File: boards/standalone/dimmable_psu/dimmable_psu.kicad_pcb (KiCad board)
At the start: 2 copper layers, 78 parts, among them J1 DIM_IN, J2 PWM_IN, J3 POWER, J4 POWER_OUT, Q1 2N7002, Q2 IRF540N, Q3 IRF540N, U1 LM324, U2 LMC7660, U3 TPS92640

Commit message: proper footprint for opamp
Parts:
- U1: footprint Package_SO:SO-14_3.9x8.65mm_P1.27mm -> Package_SO:SOIC-14_3.9x8.7mm_P1.27mm

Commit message: mounting holes!
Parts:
- added H1: MountingHole_Pad, MountingHole:MountingHole_3.2mm_M3_Pad, F.Cu at (4.00, 4.00)
- added H2: MountingHole_Pad, MountingHole:MountingHole_3.2mm_M3_Pad, F.Cu at (96.0, 4.00)
- added H3: MountingHole_Pad, MountingHole:MountingHole_3.2mm_M3_Pad, F.Cu at (96.0, 46.0)
- added H4: MountingHole_Pad, MountingHole:MountingHole_3.2mm_M3_Pad, F.Cu at (4.00, 46.0)
- moved C2 147.9 mm to (27.7, 36.0)
- moved J1 147.9 mm to (10.7, 22.0)
- moved J2 147.9 mm to (10.7, 14.5)
- moved J3 147.9 mm to (8.24, 33.0)
- moved L1 51.9 mm to (82.0, 25.0), turned to 90 degrees
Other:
- board outline added: 100 x 50 mm

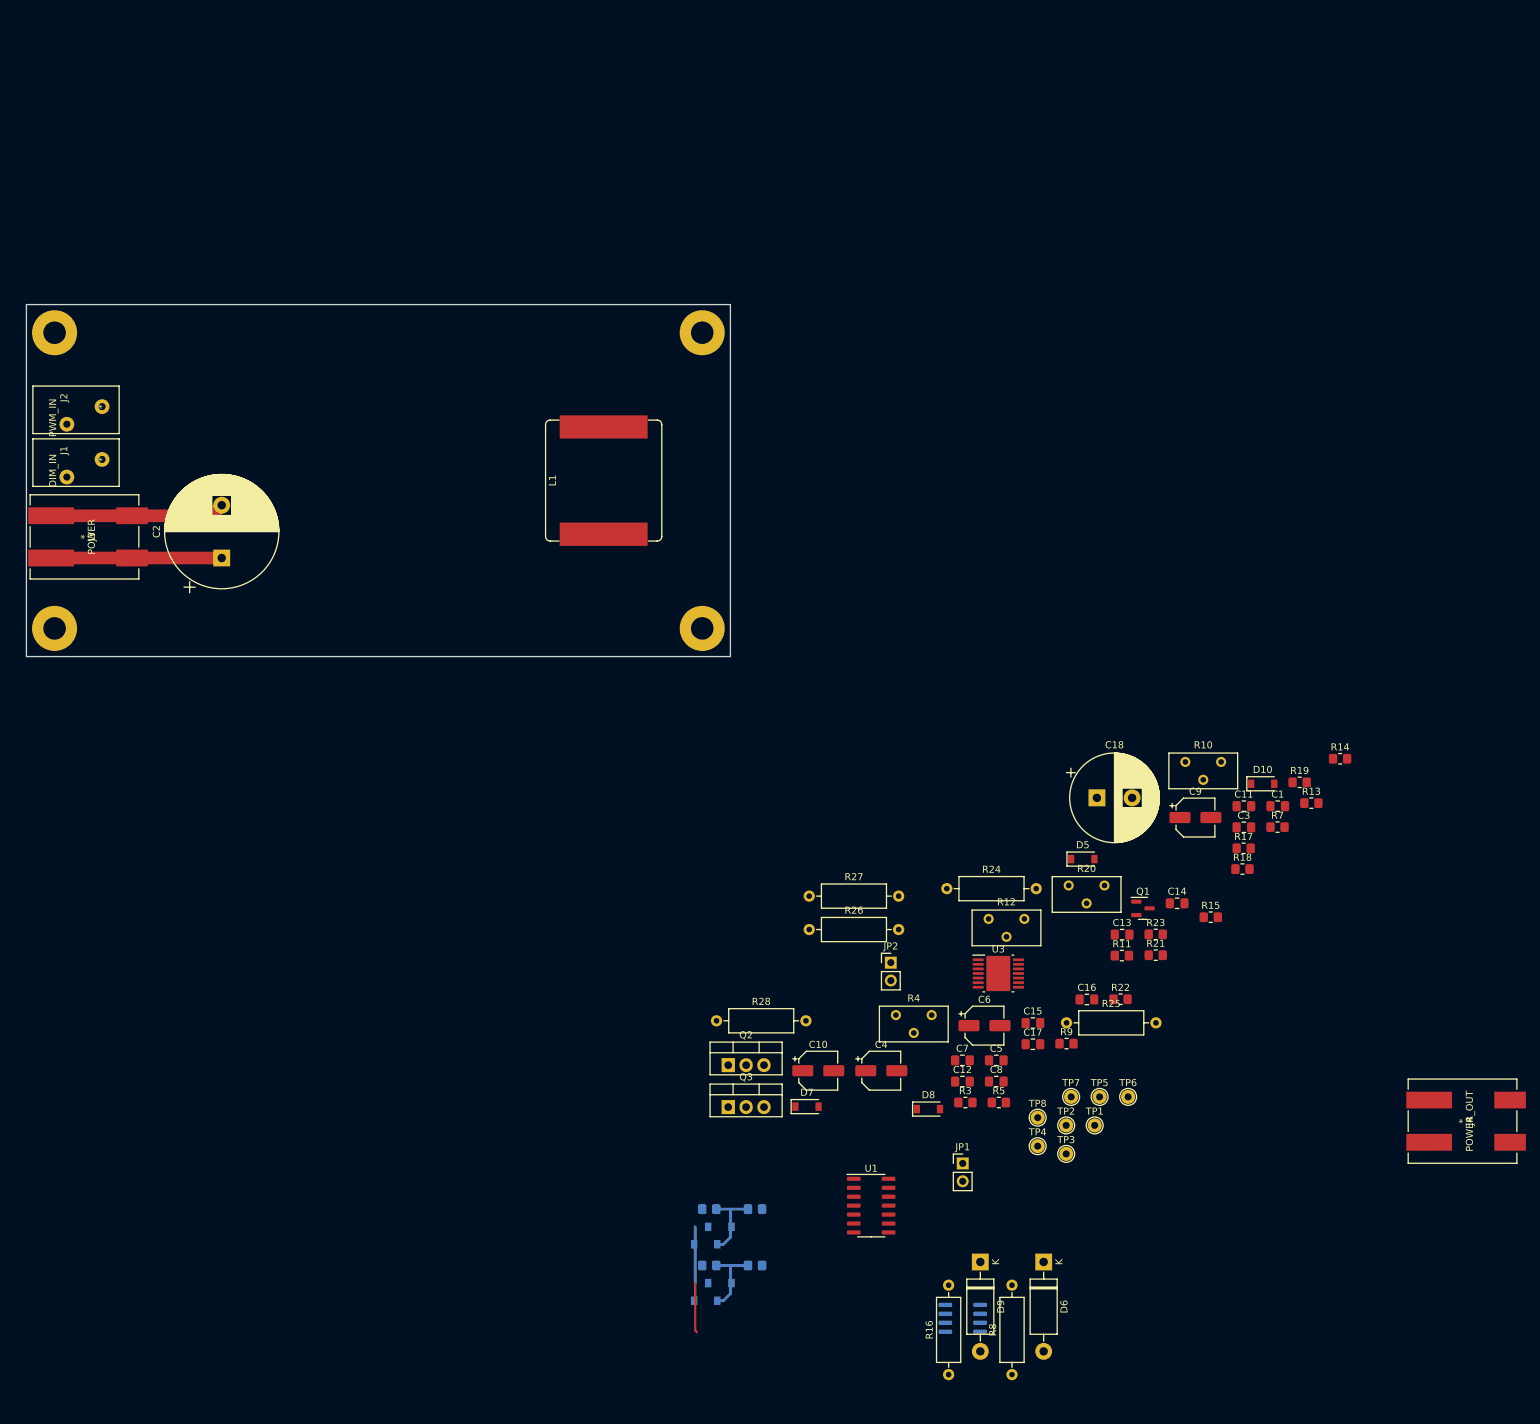
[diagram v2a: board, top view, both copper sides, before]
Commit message: arrange power-side stuff
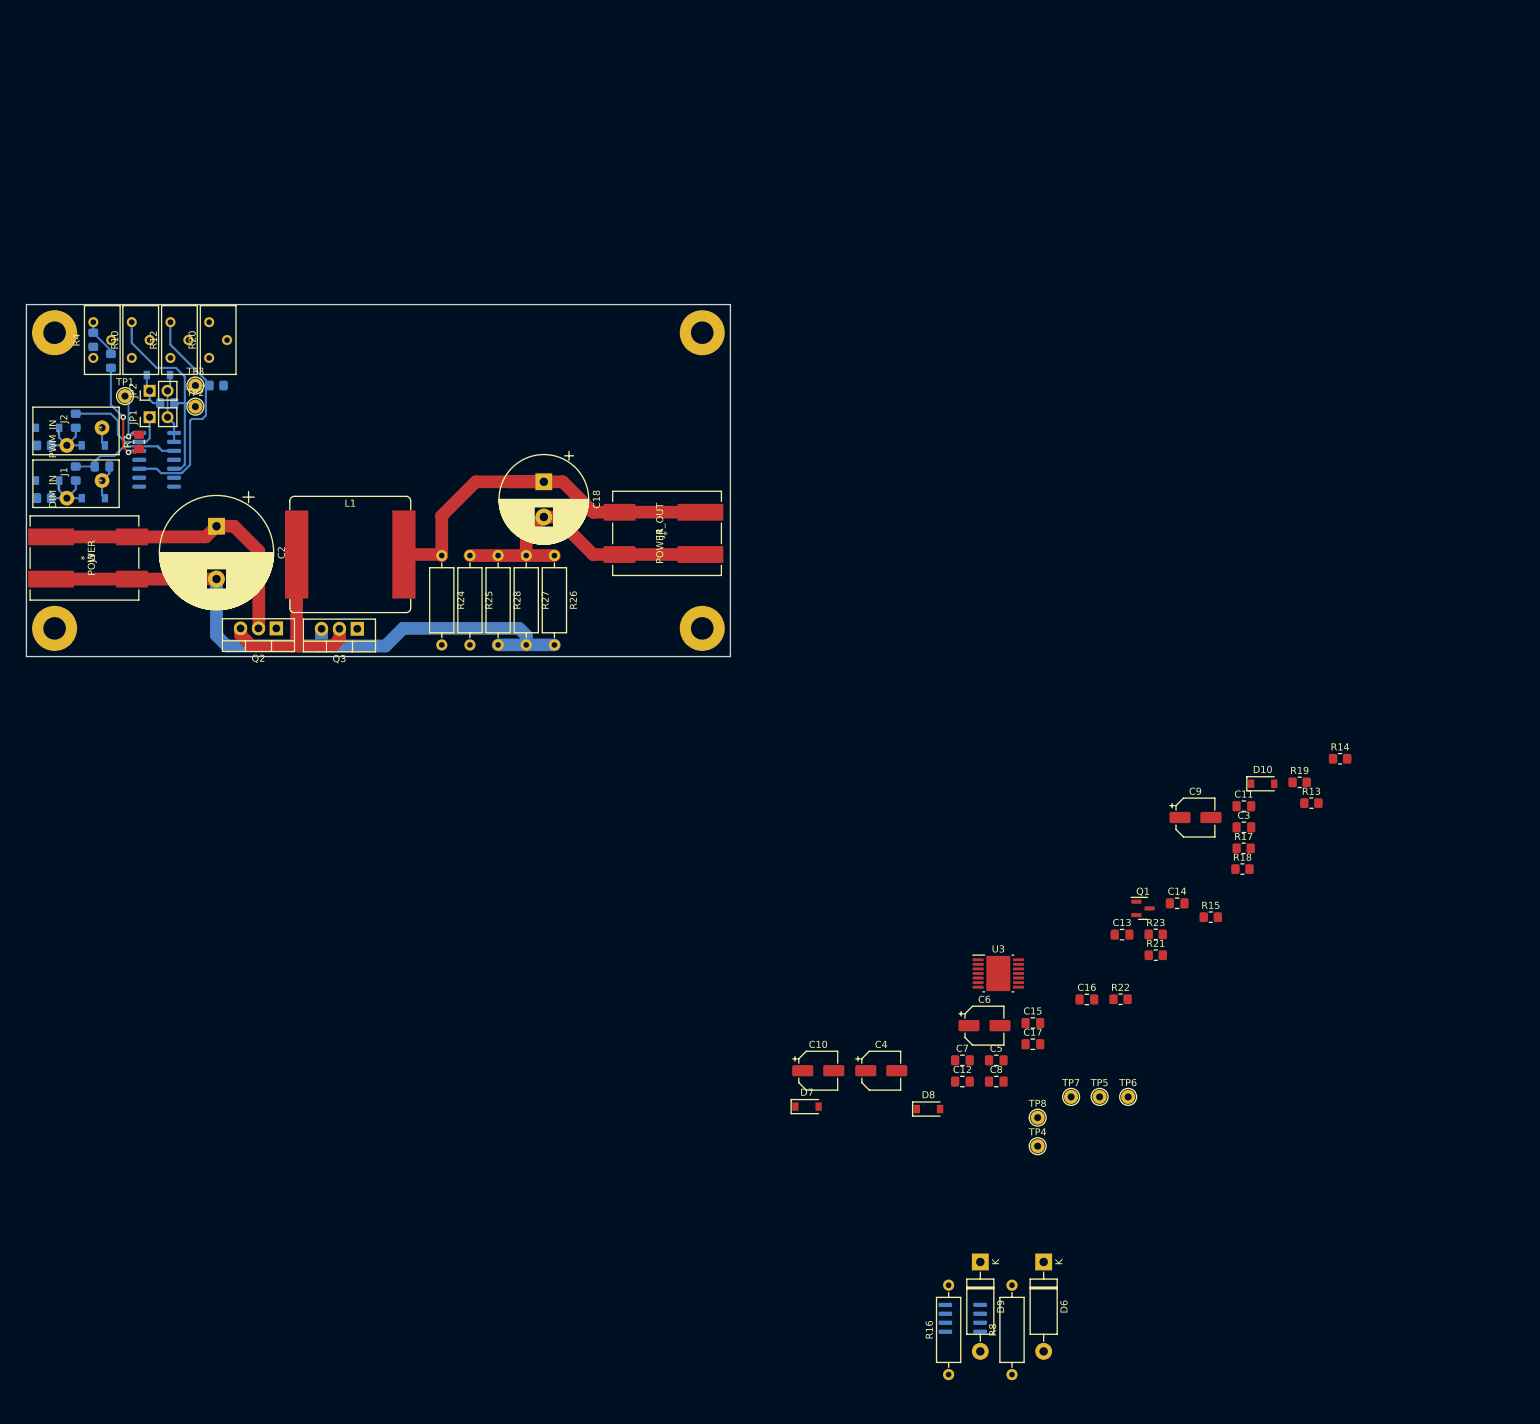
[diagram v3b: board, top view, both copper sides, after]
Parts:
- C1, D5, R11, R3, R5, R9, U1: moved to B.Cu
- moved C1 173.8 mm to (10.8, 23.0)
- moved TP1 172.4 mm to (14.0, 13.0)
- moved R7 170.7 mm to (16.0, 19.5), turned to 90 degrees
- moved R10 166.9 mm to (15.0, 2.50), turned to 90 degrees
- moved TP3 165.0 mm to (24.0, 11.5)
- moved R3 164.6 mm to (9.50, 5.00), turned to 90 degrees
- moved R5 164.3 mm to (12.0, 8.00), turned to -90 degrees
- moved TP2 160.4 mm to (24.0, 14.5)
- moved R9 156.8 mm to (20.0, 14.0)
- moved JP1 156.8 mm to (17.5, 16.0), turned to 90 degrees
- moved R4 154.5 mm to (9.50, 2.50), turned to 90 degrees
- moved R11 152.0 mm to (27.0, 11.5), turned to 180 degrees
- moved R20 150.3 mm to (26.0, 2.50), turned to 90 degrees
- moved D1 148.7 mm to (3.00, 25.0)
- moved D3 148.3 mm to (3.00, 17.5)
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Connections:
- net Net-(C16-Pad1) renamed /POWER_JUN
- C18 pad 1: Net-(C18-Pad1) -> /OUT+
- C18 pad 2: Net-(C18-Pad2) -> /OUT-
- J3 pad 1: GND -> VPP
- J3 pad 2: VPP -> GND
- J4 pad 1: Net-(C18-Pad1) -> /OUT-
- J4 pad 2: Net-(C18-Pad2) -> /OUT+
- JP2 pad 1: Net-(D5-Pad2) -> Net-(D5-Pad1)
- JP2 pad 2: Net-(D5-Pad1) -> Net-(D5-Pad2)
- L1 pad 2: Net-(C18-Pad1) -> /OUT+
- R19 pad 1: Net-(C18-Pad1) -> /OUT+
- R24 pad 1: Net-(C18-Pad1) -> /OUT+
- R24 pad 2: Net-(R24-Pad2) -> /CSENSE
- R25 pad 1: Net-(R24-Pad2) -> /OUT-
- R25 pad 2: Net-(C18-Pad2) -> /CSENSE
- R26 pad 1: Net-(C18-Pad2) -> /OUT-
- R27 pad 1: Net-(C18-Pad2) -> /OUT-
- R28 pad 1: Net-(C18-Pad2) -> /OUT-
- U3 pad 9: Net-(R24-Pad2) -> /CSENSE
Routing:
- net /OUT+: track 0.00 -> 57.2 mm
- net GND: track 42.5 -> 97.3 mm
- net /OUT-: track 0.00 -> 43.0 mm
- net /IADJ_LIMIT: track 0.00 -> 33.6 mm
- net /POWER_JUN: track 0.00 -> 30.7 mm
- net /IADJ_DIM: track 0.00 -> 29.7 mm
- net VPP: track 24.2 -> 42.6 mm
- net Net-(JP1-Pad1): track 0.00 -> 16.6 mm
- net Net-(R5-Pad2): track 0.00 -> 16.4 mm, vias 0 -> 2
- net Net-(C1-Pad1): track 0.00 -> 16.3 mm
- net Net-(D5-Pad2): track 0.00 -> 10.0 mm
- net Net-(R13-Pad1): track 0.00 -> 9.30 mm, vias 0 -> 1
- net Net-(R3-Pad2): track 0.00 -> 5.54 mm
- net Net-(D5-Pad1): track 0.00 -> 5.37 mm

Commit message: some more pcb work
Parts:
- C3, R22, R23, U3: moved to B.Cu
- moved D6 205.3 mm to (15.5, -23.6)
- moved D9 205.3 mm to (6.50, -23.6)
- moved R16 205.3 mm to (2.00, -7.65)
- moved R8 205.3 mm to (11.0, -7.65)
- moved U2 205.3 mm to (4.00, -15.7)
- moved C10 155.1 mm to (28.4, -21.4)
- moved C12 155.1 mm to (48.8, -19.9)
- moved C15 155.1 mm to (58.8, -28.2)
- moved C17 155.1 mm to (58.8, -25.2)
- moved C4 155.1 mm to (37.3, -21.4)
- moved C5 155.1 mm to (53.6, -22.9)
- moved C6 155.1 mm to (52.0, -27.9)
- moved C7 155.1 mm to (48.8, -22.9)
- moved C8 155.1 mm to (53.6, -19.9)
- moved D7 155.1 mm to (26.8, -16.4)
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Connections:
- U3 pad 15: (no net) -> GND
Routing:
- net /CSENSE: track 0.00 -> 27.4 mm, vias 0 -> 1
- net GND: track 97.3 -> 119.9 mm
- net /POWER_JUN: track 30.7 -> 35.6 mm, vias 0 -> 1
- net /OUT-: track 43.0 -> 47.8 mm
- net VPP: track 42.6 -> 46.9 mm, vias 0 -> 1
- net Net-(Q2-Pad1): track 0.00 -> 3.54 mm
- net Net-(R22-Pad1): track 0.00 -> 2.70 mm
- net Net-(Q3-Pad1): track 0.00 -> 2.52 mm
- net /OUT+: track 57.2 -> 59.2 mm

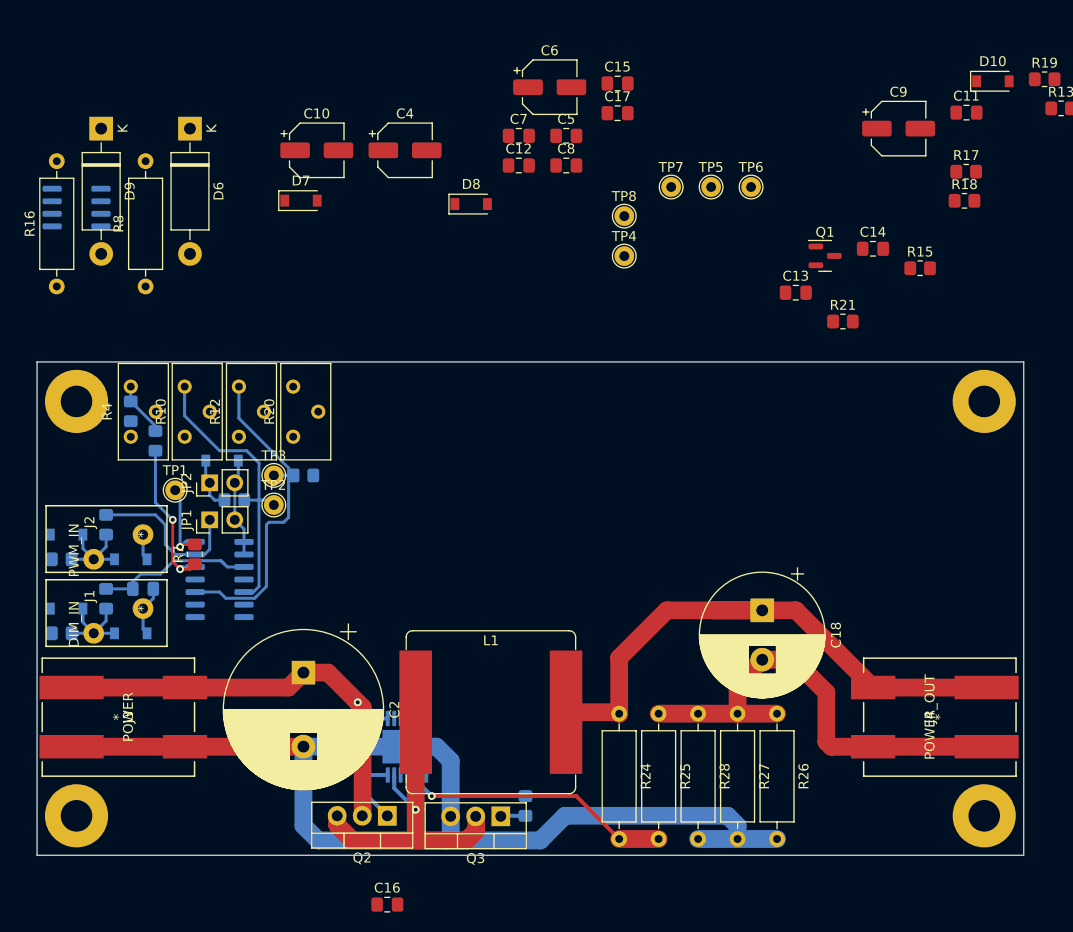
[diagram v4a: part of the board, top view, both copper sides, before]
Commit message: use dip switches instead of jumpers
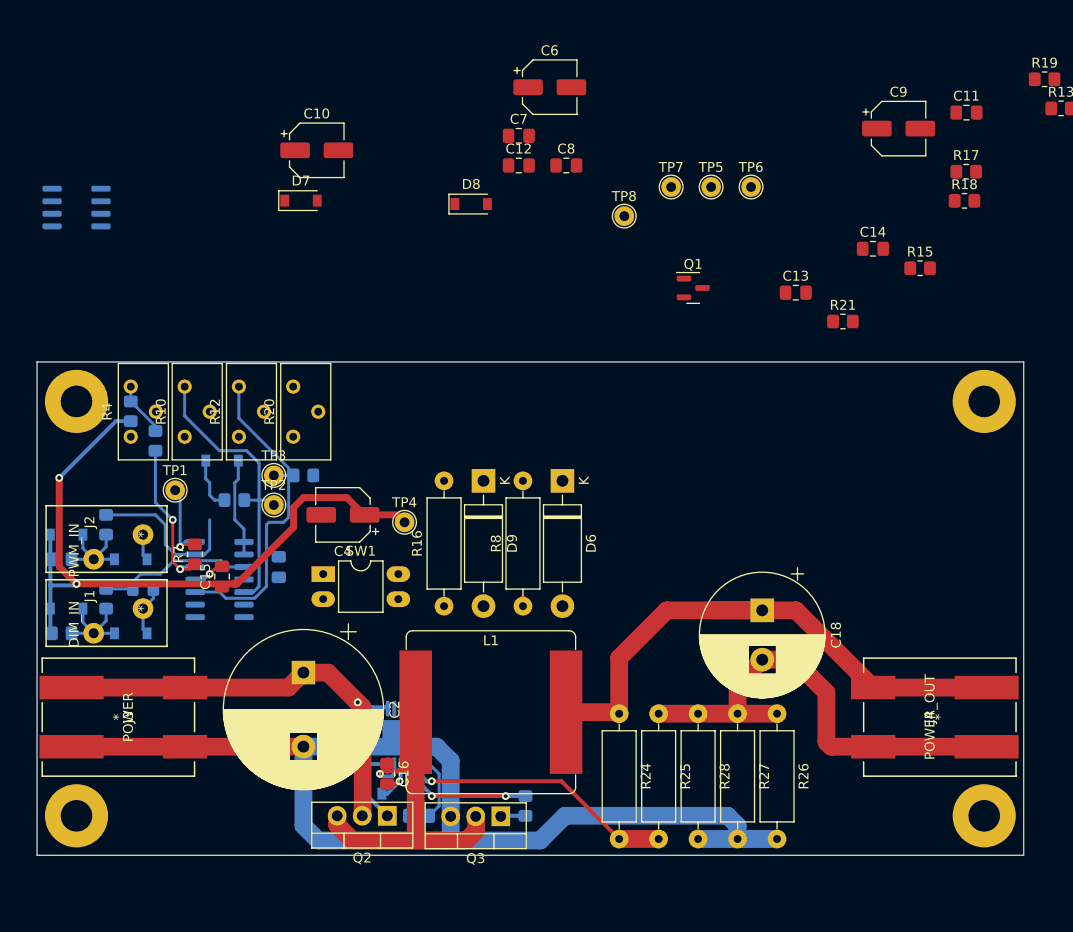
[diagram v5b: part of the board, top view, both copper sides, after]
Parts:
- removed JP1: AUTO_OFF, Connector_PinHeader_2.54mm:PinHeader_1x02_P2.54mm_Vertical
- removed JP2: ~ZERO_OFFSET, Connector_PinHeader_2.54mm:PinHeader_1x02_P2.54mm_Vertical
- added SW1: SW_DIP_SPLIT_x02, Package_DIP:DIP-4_W7.62mm_LongPads, F.Cu at (29.0, 21.5)
- C17, C5, D10: moved to B.Cu
- moved D10 94.0 mm to (36.6, 43.8)
- moved C17 74.0 mm to (38.7, 46.0)
- moved C15 64.1 mm to (18.8, 21.8), turned to 90 degrees
- moved D9 52.7 mm to (45.2, 12.1)
- moved C5 52.5 mm to (24.5, 20.8), turned to 90 degrees
- moved D6 52.0 mm to (53.2, 12.1)
- moved R16 50.9 mm to (41.2, 24.8)
- moved R8 50.1 mm to (49.2, 24.8)
- moved C4 37.5 mm to (31.0, 15.5), turned to 180 degrees
- moved TP4 35.0 mm to (37.2, 16.2)
- moved Q1 13.8 mm to (66.5, -7.50)
- moved C16 13.2 mm to (35.5, 41.8), turned to -90 degrees
- moved U3 1.00 mm to (37.5, 38.0)
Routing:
- net VDD: track 0.00 -> 72.5 mm, vias 0 -> 2
- net Net-(R23-Pad1): track 0.00 -> 13.4 mm, vias 0 -> 2
- net /POWER_JUN: track 35.6 -> 42.7 mm
- net GND: track 119.9 -> 126.2 mm
- net Net-(C17-Pad1): track 0.00 -> 5.69 mm
- net Net-(C16-Pad2): track 0.00 -> 5.37 mm, vias 0 -> 1
- net -VSW: track 0.00 -> 3.28 mm, vias 0 -> 1
- net VPP: track 46.9 -> 48.3 mm
